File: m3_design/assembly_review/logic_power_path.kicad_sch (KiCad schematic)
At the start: 19 parts, among them U10 TPS2553DBVR, U11 TPS2121RUXR

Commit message: R10: m3_design/r10_build.sh and per-family stage gate; m3_design/assembly_review rebuilt as M3-ASSY-R10 (board 883d2db5..., 46 x 90 mm); tools/check.sh passes at zero; binding note bound to the board
Co-Authored-By: Claude Opus 5.5 <noreply@anthropic.com>
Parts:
- C84: value 330uF 35V -> 470uF 25V polymer; footprint rocket:M3_OSCON_F12 -> rocket:M3_MA_8x10; LCSC C178373 -> C46550466; LCSC Part C178373 -> (none); Manufacturer Panasonic -> jieerrui; Manufacturer Part 35SVPK330M -> MA25V470M8x10
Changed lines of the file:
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@@
 		(title "08 | USB limit, source mux and hold-up")
 		(date "2026-10-12")
-		(rev "M3-ASSY-R9")
+		(rev "M3-ASSY-R10")
 		(company "Single-board M3 candidate; full system incomplete"))
 	(text "08 | USB limit, source mux and hold-up"
@@
 )
 	(symbol
-		(lib_id "M3:PolarCap")
-		(at 360.68 127 0)
-		(unit 1)
-		(in_bom yes)
-		(on_board yes)
-		(dnp no)
-		(property "Reference" "C84"
-			(at 360.68 115.57 0)
-			(effects
-				(font
-					(size 1.27 1.27))))
-		(property "Value" "330uF 35V"
-			(at 360.68 119.38 0)
-			(effects
-				(font
-					(size 1.27 1.27))))
-		(property "Footprint" "rocket:M3_OSCON_F12"
-			(at 360.68 127 0)
-			(hide yes)
-			(effects
-				(font
-					(size 1.27 1.27))))
-		(property "Datasheet" ""
-			(at 360.68 127 0)
-			(hide yes)
-			(effects
-				(font
-					(size 1.27 1.27))))
-		(property "LCSC" "C178373"
-			(at 360.68 127 0)
-			(hide yes)
-			(effects
-				(font
-					(size 1.27 1.27))))
-		(property "LCSC Part" "C178373"
-			(at 360.68 127 0)
-			(hide yes)
-			(effects
-				(font
-					(size 1.27 1.27))))
-		(property "Manufacturer" "Panasonic"
-			(at 360.68 127 0)
-			(hide yes)
-			(effects
-				(font
-					(size 1.27 1.27))))
-		(property "Manufacturer Part" "35SVPK330M"
-			(at 360.68 127 0)
-			(hide yes)
-			(effects
-				(font
-					(size 1.27 1.27))))
-		(instances
-			(project "m3"
-				(path "/6007a7db-6a58-5660-8beb-956dea045ff8/98c21473-b271-5039-bfe5-b3672097f1da"
-					(reference "C84")
-					(unit 1)))))
-	(wire
-		(pts
-			(xy 360.68 123.19)
-			(xy 353.06 123.19))
-		(stroke
-			(width 0)
-			(type default))
-)
-	(global_label "VLOGIC"
-		(shape passive)
-		(at 353.06 123.19 0)
-		(effects
-			(font
-				(size 1.05 1.05))
-			(justify right))
-)
-	(wire
-		(pts
-			(xy 360.68 130.81)
-			(xy 353.06 130.81))
-		(stroke
-			(width 0)
-			(type default))
-)
-	(global_label "GND"
-		(shape passive)
-		(at 353.06 130.81 0)
-		(effects
-			(font
-				(size 1.05 1.05))
-			(justify right))
-)
-	(symbol
 		(lib_id "M3:C")
 		(at 309.88 127 0)
@@
 			(justify left))
 )
+	(symbol
+		(lib_id "M3:PolarCap")
+		(at 360.68 127 0)
+		(unit 1)
+		(in_bom yes)
+		(on_board yes)
+		(dnp no)
+		(property "Reference" "C84"
+			(at 363.22 125.73 0)
+			(effects
+				(font
+					(size 1.27 1.27))
+				(justify left)))
+		(property "Value" "470uF 25V polymer"
+			(at 363.22 128.27 0)
+			(effects
+				(font
+					(size 1.27 1.27))
+				(justify left)))
+		(property "Footprint" "rocket:M3_MA_8x10"
+			(at 360.68 127 0)
+			(hide yes)
+			(effects
+				(font
+					(size 1.27 1.27))
+				(justify left)))
+		(property "Datasheet" "https://atta.szlcsc.com/upload/public/pdf/source/20260306/24758A4FC016E80367B87853635CDCC1.pdf"
+			(at 360.68 127 0)
+			(hide yes)
+			(effects
+				(font
+					(size 1.27 1.27))
+				(justify left)))
+		(property "LCSC" "C46550466"
+			(at 360.68 127 0)
+			(hide yes)
+			(effects
+				(font
+					(size 1.27 1.27))
+				(justify left)))
+		(property "Manufacturer" "jieerrui"
+			(at 360.68 127 0)
+			(hide yes)
+			(effects
+				(font
+					(size 1.27 1.27))
+				(justify left)))
+		(property "Manufacturer Part" "MA25V470M8x10"
+			(at 360.68 127 0)
+			(hide yes)
+			(effects
+				(font
+					(size 1.27 1.27))
+				(justify left)))
+		(instances
+			(project "m3"
+				(path "/6007a7db-6a58-5660-8beb-956dea045ff8/98c21473-b271-5039-bfe5-b3672097f1da"
+					(reference "C84")
+					(unit 1)))))
+	(wire
+		(pts
+			(xy 360.68 123.19)
+			(xy 360.68 118.11))
+		(stroke
+			(width 0)
+			(type default))
+)
+	(global_label "VLOGIC"
+		(shape passive)
+		(at 360.68 118.11 0)
+		(effects
+			(font
+				(size 1.05 1.05))
+			(justify right))
+)
+	(wire
+		(pts
+			(xy 360.68 130.81)
+			(xy 360.68 135.89))
+		(stroke
+			(width 0)
+			(type default))
+)
+	(global_label "GND"
+		(shape passive)
+		(at 360.68 135.89 0)
+		(effects
+			(font
+				(size 1.05 1.05))
+			(justify right))
+)
 	(sheet_instances

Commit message: R10 requirements-audit cuts and GAP fixes before review round 9
Implement adopted AUD-1 through AUD-10 and GAP-1 through GAP-5 after the single-switch pass.
Remove the advisory pull-pin, redundant probes and GPS/radio IO LDO cells; qualify the smaller
AONR21357 pair, correct C120 voltage rating, standardize shared-code capacitor lands, simplify
slow returns and fire-only copper, localize U9 output protection and add exactly two U401 VIPPO vias.
Record physical-current timing, coupled fire/source budget, C84 manual fitting and narrowed gate scopes.

Board SHA-256: 877d01996a59e9dd5c6dbc367274bb9a323a13982d67960fe46df9b0ee53205d
Board: 46 x 90 mm, 4 layers, 2365477 bytes; 225 footprints, 883 straight tracks, 323 vias.
Netlist SHA-256: 0843da709e2d7a757e9b35cdff48158a54012c5353619cbf409ab961efd2c3ca
Two fresh complete passing builds are byte-identical. Schematic: 700 pins; 22 seeded faults detected.

Final unskipped tools/check.sh: exit 0
DRC violations 0  unconnected 0  schematic parity 0  ERC 0
metadata / 3D model audit: OK
silkscreen outside the board outline: 0 stroke points
fit check: OK (CAD envelopes only)
R10 CAD contract (full): OK
routing hygiene: 0 failing, 0 allowlisted, 0 leftovers recorded
actuator safety contract: OK
Fab manifest: OK; 5 outputs match current CAD and export inputs
Self-tests: shell 4, fit 24, paste 5, routing 59, R10 131; three NumPy cases rerun and passed.

Fab: 215 CPL rows, 82 BOM codes; orientation / paste / manifest pass. Hot-plug: 2304 required
cases plus convergence and controls pass (simulation / Inference). Plate f1 280.9 Hz (Inference).
Live JLC: $84.43 vs $84.41 target, 46 Extended codes; R430 / U4 short. Procurement exit 1 is a
disclosed OQ-3 / ordering deviation, not a CAD gate pass. No quote accepted or order placed.
Firmware, bench, thermal/transient correlation, process acceptance, installed RF immunity and physical fit unverified.

This preparatory pass earns no clean-review credit. Start fresh full ten-lens round 9 on th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
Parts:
- removed TP86: USB_FAULT_N, rocket:M3_TestPad_1.5, symbol M3:TestPoint
- removed TP87: LOGIC_SOURCE_ST, rocket:M3_TestPad_1.5, symbol M3:TestPoint
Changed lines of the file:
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@@
-			(justify right))
-)
-	(symbol
-		(lib_id "M3:TestPoint")
-		(at 223.52 213.36 0)
-		(unit 1)
-		(in_bom no)
-		(on_board yes)
-		(dnp no)
-		(property "Reference" "TP86"
-			(at 223.52 205.74 0)
-			(effects
-				(font
-					(size 1.27 1.27))))
-		(property "Value" "USB_FAULT_N"
-			(at 223.52 209.55 0)
-			(effects
-				(font
-					(size 1.27 1.27))))
-		(property "Footprint" "rocket:M3_TestPad_1.5"
-			(at 223.52 213.36 0)
-			(hide yes)
-			(effects
-				(font
-					(size 1.27 1.27))))
-		(property "Datasheet" ""
-			(at 223.52 213.36 0)
-			(hide yes)
-			(effects
-				(font
-					(size 1.27 1.27))))
-		(property "LCSC" ""
-			(at 223.52 213.36 0)
-			(hide yes)
-			(effects
-				(font
-					(size 1.27 1.27))))
-		(instances
-			(project "m3"
-				(path "/6007a7db-6a58-5660-8beb-956dea045ff8/98c21473-b271-5039-bfe5-b3672097f1da"
-					(reference "TP86")
-					(unit 1)))))
-	(wire
-		(pts
-			(xy 223.52 213.36)
-			(xy 215.9 213.36))
-		(stroke
-			(width 0)
-			(type default))
-)
-	(global_label "USB_FAULT_N"
-		(shape passive)
-		(at 215.9 213.36 0)
-		(effects
-			(font
-				(size 1.05 1.05))
-			(justify right))
-)
-	(symbol
-		(lib_id "M3:TestPoint")
-		(at 330.2 213.36 0)
-		(unit 1)
-		(in_bom no)
-		(on_board yes)
-		(dnp no)
-		(property "Reference" "TP87"
-			(at 330.2 205.74 0)
-			(effects
-				(font
-					(size 1.27 1.27))))
-		(property "Value" "LOGIC_SOURCE_ST"
-			(at 330.2 209.55 0)
-			(effects
-				(font
-					(size 1.27 1.27))))
-		(property "Footprint" "rocket:M3_TestPad_1.5"
-			(at 330.2 213.36 0)
-			(hide yes)
-			(effects
-				(font
-					(size 1.27 1.27))))
-		(property "Datasheet" ""
-			(at 330.2 213.36 0)
-			(hide yes)
-			(effects
-				(font
-					(size 1.27 1.27))))
-		(property "LCSC" ""
-			(at 330.2 213.36 0)
-			(hide yes)
-			(effects
-				(font
-					(size 1.27 1.27))))
-		(instances
-			(project "m3"
-				(path "/6007a7db-6a58-5660-8beb-956dea045ff8/98c21473-b271-5039-bfe5-b3672097f1da"
-					(reference "TP87")
-					(unit 1)))))
-	(wire
-		(pts
-			(xy 330.2 213.36)
-			(xy 322.58 213.36))
-		(stroke
-			(width 0)
-			(type default))
-)
-	(global_label "LOGIC_SOURCE_ST"
-		(shape passive)
-		(at 322.58 213.36 0)
-		(effects
-			(font
-				(size 1.05 1.05))
 			(justify right))
 )

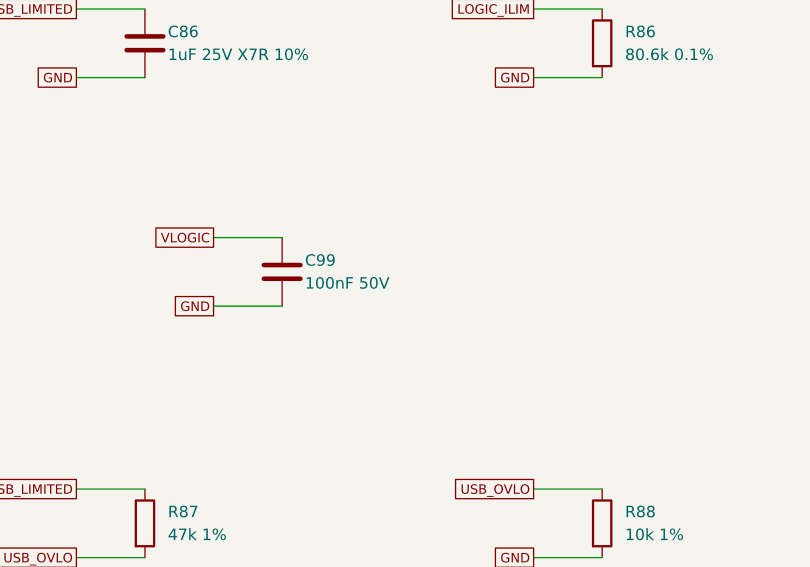
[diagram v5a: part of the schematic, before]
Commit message: Finish R10 round 9 Minor fix pass
Complete the interrupted generator rebuild and apply the recorded round 9
Minor fixes: capacitor labels, cold-screen ordering, debugger instructions,
local route cleanups, gate fault detection and explicit R10 procurement limits.
Refresh the board-bound fabrication, supplier and validation records.

Round 9 reviewed 8bccb07: 0 Critical, 0 Major, 21 Minor groups. Round 10 will
freshly review this committed fix pass, including every changed CAD item.

Board SHA-256: b337fe63c258c85ba4120e75ad018afa0c22241f8bc21a4172787cf2887208d9
Board: 46 x 90 mm, 2366509 bytes. Two COMPLETE builds pass; all 21 generated
CAD and binding files are byte-identical.

Unskipped tools/check.sh: exit 0.
DRC violations 0; unconnected 0; schematic parity 0; ERC 0.
Metadata / 3D, silk, fit / plate, all 33 R10 rules, routing hygiene, actuator
contract and current 5-output fabrication manifest: OK.
Self-tests: shell 4, procurement 19, fit 24, paste 5, routing 59, R10 140;
3 NumPy cases rerun successfully, no unresolved skips. Hot-plug: 2304/2304
required cases pass (simulation / Inference).

Fab export, required fitting, orientation and paste pass: 215 CPL rows,
82 BOM codes. Fresh supplier/procurement checks correctly FAIL the known
$84.43 versus $84.41 cap and R430/U4 stock shortages; 46 Extended codes.
OQ-3 and final deviation acceptance remain pending. No firmware, bench,
installed RF immunity, physical fit, assembly-process or flight result claimed.

Evidence: docs/R10_VALIDATION.md and sources/r10_review/round9_fix_validation.json
and round9_fix_check.txt under m3_design/assembly_review. Native headless
KiCad environment uses the external D-R1-05 mouse-query workaround only;
repository gates and CAD rules are unchanged by that workaround.

Co-Authored-By: Claude Opus 5.5 <noreply@anthropic.com>
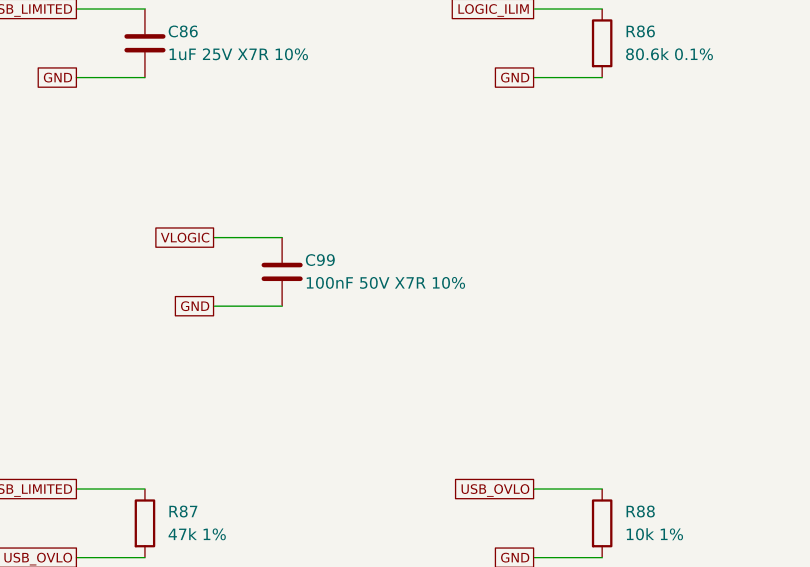
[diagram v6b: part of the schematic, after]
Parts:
- C99: value 100nF 50V -> 100nF 50V X7R 10%
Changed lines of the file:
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@@
 					(size 1.27 1.27))
 				(justify left)))
-		(property "Value" "100nF 50V"
+		(property "Value" "100nF 50V X7R 10%"
 			(at 226.0600 153.6700 0)
 			(effects
